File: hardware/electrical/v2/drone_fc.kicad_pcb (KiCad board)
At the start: 0 parts

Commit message: schematic: add MCU decoupling, IMU CS pull-up and INT2 pin
Drops the analog CURRENT_SENSE net: the ESC reports pack current over its serial telemetry, so a second path to the same shunt earned nothing and cost an ADC pin. J1 pin 6 and the MCU ADC pin are marked no-connect. Adds decoupling the module supply was missing entirely (4.7 uF bulk plus 100 nF per rail), a 1 uF local input cap at the LDO, and a 10k pull-up on IMU_CS so the IMU does not see spurious SPI while the MCU is in reset. Adds the missing INT2 pin 14 to the ICM-42688-P symbol, which is a 14-pad part, and marks it no-connect. ERC is clean: 0 errors, remaining warnings are library sync only. PCB layout is still work in progress and has known DRC violations.
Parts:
- added C1: 100nF_BOOT, Capacitor_SMD:C_0402_1005Metric, F.Cu at (63.0, 104.9)
- added C10: 1uF, Capacitor_SMD:C_0603_1608Metric, F.Cu at (56.1, 110.4)
- added C2: 10uF_50V, Capacitor_SMD:C_0805_2012Metric, F.Cu at (71.8, 104.6)
- added C3: 22uF_10V, Capacitor_SMD:C_0805_2012Metric, F.Cu at (71.8, 107.6)
- added C5: 100nF, Capacitor_SMD:C_0402_1005Metric, F.Cu at (63.0, 106.9)
- added C6: 10nF, Capacitor_SMD:C_0402_1005Metric, F.Cu at (63.0, 108.8)
- added D1: Green_Status, LED_SMD:LED_0402_1005Metric, F.Cu at (59.8, 110.1)
- added D2: Blue_Radio, LED_SMD:LED_0402_1005Metric, F.Cu at (59.8, 112.1)
- added J1: ESC_4IN1_JST_SH, drone_fc_v2_footprints:JST_SH_SM08B-SRSS-TB_1x08-1MP_P1.00mm_Horizontal, F.Cu at (115.0, 89.0)
- added J3: Cortex_SWD_10P, Connector_PinHeader_1.27mm:PinHeader_2x05_P1.27mm_Vertical_SMD, F.Cu at (86.0, 86.8)
- added L1: 15uH, Inductor_SMD:L_0805_2012Metric, F.Cu at (51.8, 110.5)
- added R10: 10k, Resistor_SMD:R_0402_1005Metric, F.Cu at (63.0, 98.9)
- added R11: 88.7K, Resistor_SMD:R_0402_1005Metric, F.Cu at (63.0, 100.9)
- added R12: 22.1K, Resistor_SMD:R_0402_1005Metric, F.Cu at (63.0, 102.9)
- added R3: 1k_1%, Resistor_SMD:R_0402_1005Metric, F.Cu at (63.0, 89.0)
- added R4: 1k_1%, Resistor_SMD:R_0402_1005Metric, F.Cu at (63.0, 91.0)
- added R7: 10k, Resistor_SMD:R_0402_1005Metric, F.Cu at (63.0, 93.0)
- added R8: 10k, Resistor_SMD:R_0402_1005Metric, F.Cu at (63.0, 95.0)
- added R9: 10k, Resistor_SMD:R_0402_1005Metric, F.Cu at (63.0, 97.0)
- added TVS1: SMAJ24A, Diode_SMD:D_SMA, F.Cu at (53.6, 106.8)
- added U1: MDBT53-P1M, drone_fc_v2_footprints:MDBT53-P1M, F.Cu at (100.0, 90.5)
- added U2: ICM-42688-P, drone_fc_v2_footprints:LGA-14_2.5x3.0mm_P0.5mm_ICM42688P, F.Cu at (72.0, 111.6)
- added U3: LMR50410_Buck, Package_TO_SOT_SMD:SOT-23-6, F.Cu at (67.0, 105.5)
- added U4: TLV75533PDBVR, Package_TO_SOT_SMD:SOT-23-5, F.Cu at (67.0, 110.1)
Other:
- board outline added: 38 x 38 mm
- copper layers 0 -> 4
- board text added: "ANTENNA ZONE - NO COPPER"

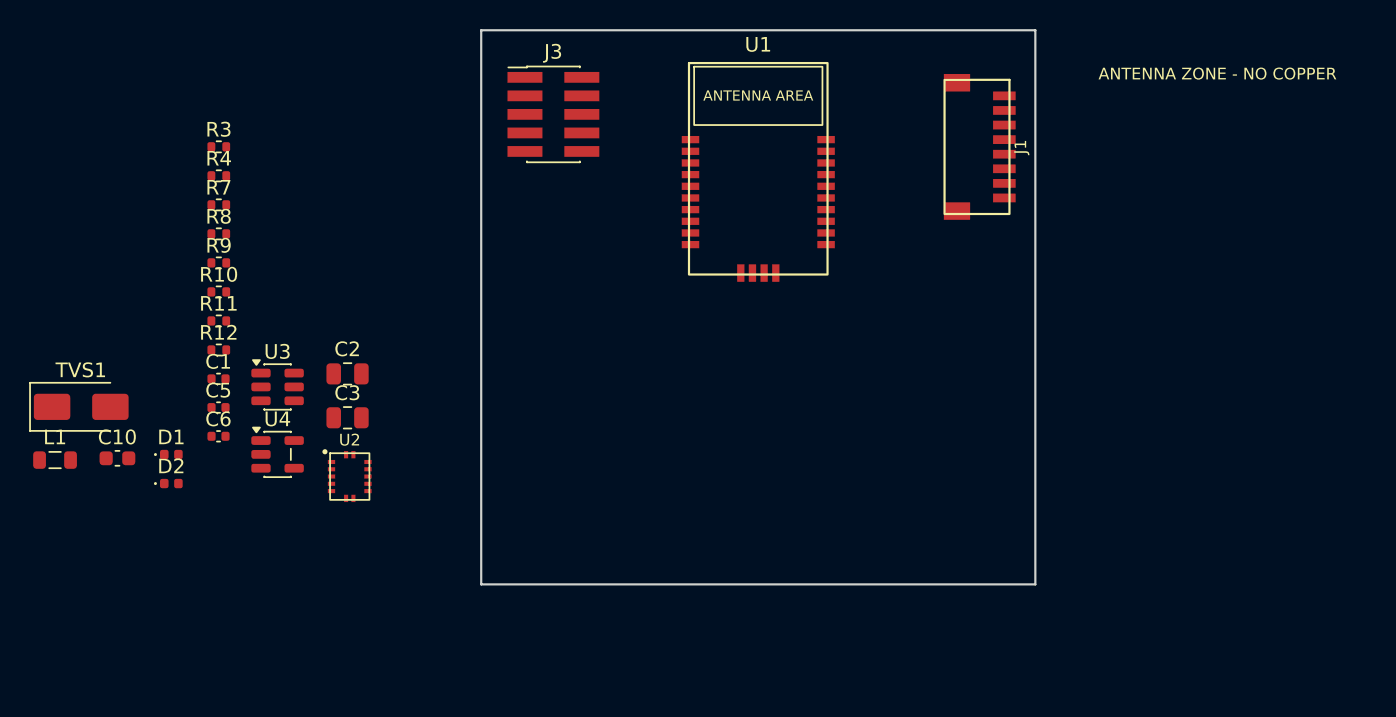
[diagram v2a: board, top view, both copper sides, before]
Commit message: layout: establish stack-compatible FC placement
Define the 20 mm ESC mounting pattern and board outline, place the flight-controller components around the stack, and preserve the MDBT53 antenna keepout at the board edge. Add labelled GND, VBAT, +4V, and +3V3 schematic test points with matching board pads. Repair the MDBT53 courtyard and route the first buck switch-node and +4V segments.\n\nERC is clean. PCB DRC has no electrical or mechanical errors; remaining findings are silkscreen-only while routing is in progress.
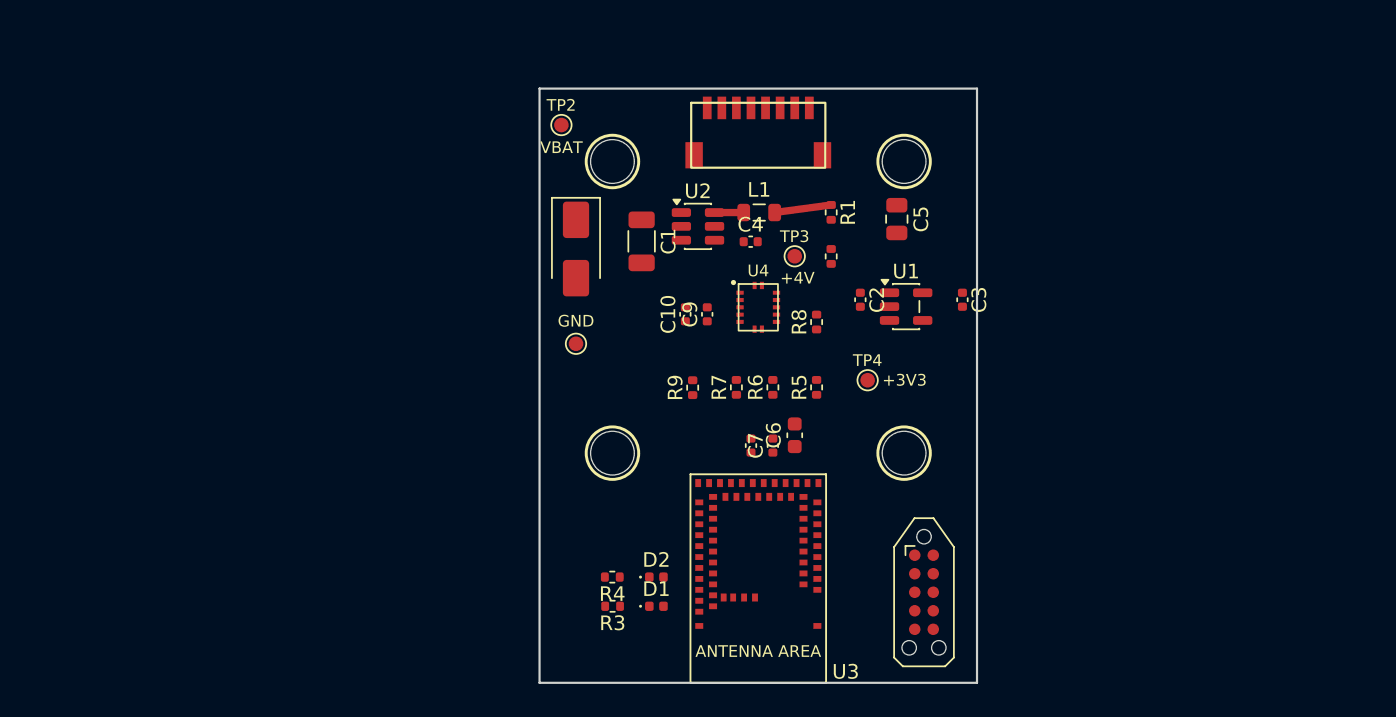
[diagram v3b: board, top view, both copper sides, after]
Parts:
- removed J3: Cortex_SWD_10P, Connector_PinHeader_1.27mm:PinHeader_2x05_P1.27mm_Vertical_SMD
- removed R10: 10k, Resistor_SMD:R_0402_1005Metric
- removed R11: 88.7K, Resistor_SMD:R_0402_1005Metric
- removed R12: 22.1K, Resistor_SMD:R_0402_1005Metric
- added C4: 100nF, Capacitor_SMD:C_0402_1005Metric, F.Cu at (99.5, 95.5)
- added C7: 100nF, Capacitor_SMD:C_0402_1005Metric, F.Cu at (101.0, 109.5)
- added C8: 100nF, Capacitor_SMD:C_0402_1005Metric, F.Cu at (99.5, 109.5)
- added C9: 100nF, Capacitor_SMD:C_0402_1005Metric, F.Cu at (96.5, 100.5)
- added H1: M2 soft mount, MountingHole_3.0mm, F.Cu at (90.0, 90.0)
- added H2: M2 soft mount, MountingHole_3.0mm, F.Cu at (110.0, 90.0)
- added H3: M2 soft mount, MountingHole_3.0mm, F.Cu at (90.0, 110.0)
- added H4: M2 soft mount, MountingHole_3.0mm, F.Cu at (110.0, 110.0)
- added J2: ESC_4IN1_JST_SH, drone_fc_v2_footprints:JST_SH_SM08B-SRSS-TB_1x08-1MP_P1.00mm_Horizontal, F.Cu at (100.0, 88.2)
- added R1: 66.5K, Resistor_SMD:R_0402_1005Metric, F.Cu at (105.0, 93.5)
- added R2: 22.1K, Resistor_SMD:R_0402_1005Metric, F.Cu at (105.0, 96.5)
- added R5: 10k, Resistor_SMD:R_0402_1005Metric, F.Cu at (104.0, 105.5)
- added R6: 10k, Resistor_SMD:R_0402_1005Metric, F.Cu at (101.0, 105.5)
- added TP1: GND, TestPoint:TestPoint_Pad_D1.0mm, F.Cu at (87.5, 102.5)
- added TP2: VBAT, TestPoint:TestPoint_Pad_D1.0mm, F.Cu at (86.5, 87.5)
- added TP3: +4V, TestPoint:TestPoint_Pad_D1.0mm, F.Cu at (102.5, 96.5)
- added TP4: +3V3, TestPoint:TestPoint_Pad_D1.0mm, F.Cu at (107.5, 105.0)
- C1: value 100nF_BOOT -> 10uF; footprint Capacitor_SMD:C_0402_1005Metric -> Capacitor_SMD:C_1206_3216Metric
- C10: value 1uF -> 10nF; footprint Capacitor_SMD:C_0603_1608Metric -> Capacitor_SMD:C_0402_1005Metric
- C2: value 10uF_50V -> 1uF; footprint Capacitor_SMD:C_0805_2012Metric -> Capacitor_SMD:C_0402_1005Metric
- C3: value 22uF_10V -> 1uF; footprint Capacitor_SMD:C_0805_2012Metric -> Capacitor_SMD:C_0402_1005Metric
- C5: value 100nF -> 22uF; footprint Capacitor_SMD:C_0402_1005Metric -> Capacitor_SMD:C_0805_2012Metric
- C6: value 10nF -> 4.7uF; footprint Capacitor_SMD:C_0402_1005Metric -> Capacitor_SMD:C_0603_1608Metric
- J1: value ESC_4IN1_JST_SH -> Cortex_SWD_10P; footprint drone_fc_v2_footprints:JST_SH_SM08B-SRSS-TB_1x08-1MP_P1.00mm_Horizontal -> Connector:Tag-Connect_TC2050-IDC-NL_2x05_P1.27mm_Vertical
- R3, R4: value 1k_1% -> 1k
- U1: value MDBT53-P1M -> TLV75533PDBVR; footprint drone_fc_v2_footprints:MDBT53-P1M -> Package_TO_SOT_SMD:SOT-23-5
- U2: value ICM-42688-P -> LMR50410_Buck; footprint drone_fc_v2_footprints:LGA-14_2.5x3.0mm_P0.5mm_ICM42688P -> Package_TO_SOT_SMD:SOT-23-6
- U3: value LMR50410_Buck -> MDBT53-P1M; footprint Package_TO_SOT_SMD:SOT-23-6 -> drone_fc_v2_footprints:MDBT53-P1M
- U4: value TLV75533PDBVR -> ICM-42688-P; footprint Package_TO_SOT_SMD:SOT-23-5 -> drone_fc_v2_footprints:LGA-14_2.5x3.0mm_P0.5mm_ICM42688P
- moved L1 51.2 mm to (100.1, 93.5)
- moved C5 48.3 mm to (109.5, 94.0), turned to -90 degrees
- moved C3 42.9 mm to (114.0, 99.5), turned to -90 degrees
- moved R3 41.5 mm to (90.0, 120.5), turned to 180 degrees
- moved R8 41.4 mm to (104.0, 101.0), turned to 90 degrees
- moved C10 40.2 mm to (95.0, 100.5), turned to 90 degrees
- moved C6 39.5 mm to (102.5, 108.8), turned to 90 degrees
- moved R4 38.5 mm to (90.0, 118.5), turned to 180 degrees
- moved R7 37.6 mm to (98.5, 105.5), turned to 90 degrees
- moved TVS1 35.6 mm to (87.5, 96.0), turned to -90 degrees
- moved C2 35.5 mm to (107.0, 99.5), turned to -90 degrees
- moved U3 35.5 mm to (100.0, 118.6)
- moved D1 34.9 mm to (93.0, 120.5)
- moved U4 34.5 mm to (100.0, 100.0)
- moved D2 33.9 mm to (93.0, 118.5)
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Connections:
- C1 pad 1: Net-(U3-SW) -> /VBAT
- C1 pad 2: Net-(U3-BOOT) -> GND
- C2 pad 1: /VBAT -> /+4V
- C3 pad 1: /+5V -> /+3V3
- C5 pad 1: /+3V3 -> /+4V
- J1 pad 1: /ESC_M4 -> /+3V3
- J1 pad 2: /ESC_M3 -> /SWDIO
- J1 pad 3: /ESC_M2 -> GND
- J1 pad 4: /ESC_M1 -> /SWDCLK
- J1 pad 5: /ESC_TLM -> GND
- J1 pad 6: /CURRENT_SENSE -> /SWO
- J1 pad 7: GND -> (no net)
- J1 pad 8: /VBAT -> (no net)
- L1 pad 1: Net-(U3-SW) -> Net-(U2-SW)
- L1 pad 2: /+5V -> /+4V
- R7 pad 1: /ESC_M4 -> /ESC_M2
- R8 pad 1: /ESC_M3 -> /+3V3
- R8 pad 2: GND -> /IMU_CS
- R9 pad 1: /ESC_M2 -> /ESC_M1
- U1 pad 1: GND -> /+4V
- U1 pad 2: /+3V3 -> GND
- U1 pad 3: /+3V3 -> /+4V
- U1 pad 5: /nRESET -> /+3V3
- U2 pad 1: /SPI_MISO -> Net-(U2-BOOT)
- U2 pad 2: /IMU_INT1 -> GND
- U2 pad 3: /+3V3 -> Net-(U2-FB)
- U2 pad 4: GND -> /VBAT
- U2 pad 5: GND -> /VBAT
- U2 pad 6: GND -> Net-(U2-SW)
- U3 pad 1: Net-(U3-BOOT) -> GND
- U3 pad 2: GND -> /SWDCLK
- U3 pad 3: Net-(U3-FB) -> /SWO
- U3 pad 4: /VBAT -> /SWDIO
- U3 pad 5: /VBAT -> unconnected-(U3-P0.27_AIN6_VBAT-Pad5)
- U3 pad 6: Net-(U3-SW) -> /nRESET
- U4 pad 1: /+5V -> /SPI_MISO
- U4 pad 3: (no net) -> GND
- U4 pad 4: (no net) -> /IMU_INT1
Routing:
- net /+4V: track 0.00 -> 3.91 mm
- net Net-(U2-SW): track 0.00 -> 2.00 mm
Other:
- board size 38 x 38 mm -> 30 x 40.8 mm
- board text removed: "ANTENNA ZONE - NO COPPER"

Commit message: layout: route ground plane and document progress
Connect the ground plane through local vias and reduce the unrouted-net count to 30. Record the Phase 4 PCB layout milestone in the project status and progress history. Remaining DRC work is limited to silkscreen cleanup and two dangling tracks.
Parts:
- moved TP4 4.47 mm to (105.5, 109.0)
- moved D1 2.25 mm to (92.0, 122.5)
- moved D2 2.25 mm to (92.0, 120.5)
- moved R3 2.25 mm to (89.0, 122.5)
- moved R4 2.25 mm to (89.0, 120.5)
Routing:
- net GND: track 0.00 -> 60.1 mm, vias 0 -> 12
- net /+3V3: track 0.00 -> 30.8 mm, vias 0 -> 3
- net /VBAT: track 0.00 -> 28.0 mm
- net /+4V: track 3.91 -> 20.7 mm
- net Net-(U2-BOOT): track 0.00 -> 7.89 mm
- net /ESC_M2: track 0.00 -> 6.52 mm
- net /ESC_M1: track 0.00 -> 6.50 mm
- added copper zone on In2.Cu, net /+3V3
- added copper zone on In1.Cu, net GND

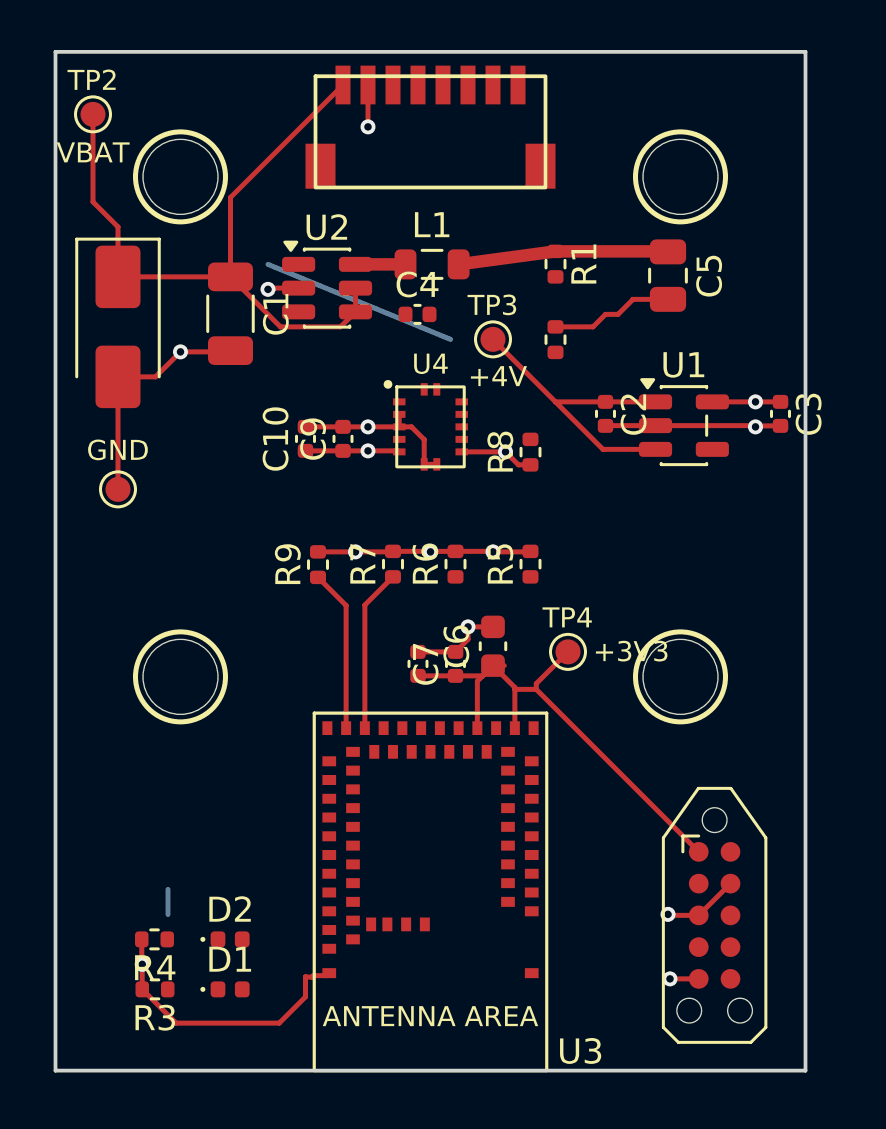
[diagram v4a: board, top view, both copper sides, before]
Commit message: layout: complete routing of the flight controller PCB
Every net on the nRF5340 carrier is now routed: 0 unconnected items, down
from 30 at the end of the previous session. No copper, clearance, short,
drill or dangling-item violations remain. The 23 outstanding DRC findings
are all silkscreen warnings - reference text over pads, label collisions
and text clipped by the board edge - which have no electrical or assembly
consequence on a 30 mm board populated with 0402s.

Also removes an accidental mirror on U2 that a crash-recovery autosave had
introduced. Mirroring a symbol relocates its pin endpoints while the wires
stay put, so every pin had swapped with its opposite across the centreline
(VIN with SW, GND with FB, BOOT with EN) - a real netlist fault rather than
a cosmetic flip. Adds the LMR50410 datasheet alongside the existing TLV755P.
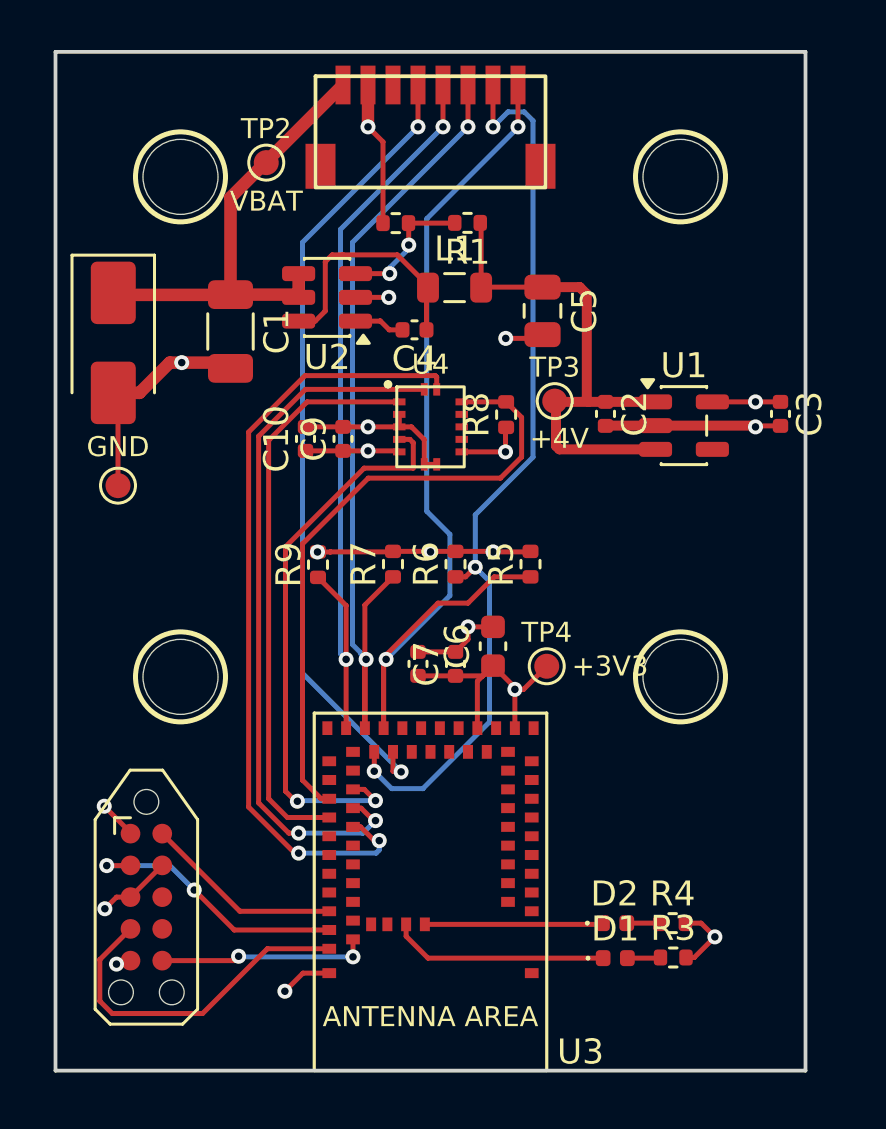
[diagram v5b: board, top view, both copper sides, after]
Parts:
- moved J1 22.7 mm to (88.6, 118.8)
- moved R3 20.8 mm to (109.7, 121.2), turned to 0 degrees
- moved R4 20.7 mm to (109.7, 119.8), turned to 0 degrees
- moved D1 15.5 mm to (107.4, 121.2)
- moved D2 15.4 mm to (107.4, 119.8)
- moved R2 7.91 mm to (98.6, 91.8), turned to 180 degrees
- moved TP2 7.19 mm to (93.4, 89.4)
- moved C5 5.21 mm to (104.5, 95.4)
- moved R1 3.89 mm to (101.5, 91.8), turned to 180 degrees
- moved TP3 3.49 mm to (105.0, 99.0)
- moved R8 1.79 mm to (103.0, 99.5)
- moved L1 1.29 mm to (101.0, 94.4)
- moved TP4 1.03 mm to (104.7, 109.6)
- moved C1 0.71 mm to (92.0, 96.2)
- moved TVS1 0.67 mm to (87.3, 96.6)
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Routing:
- net /ESC_M4: track 0.00 -> 38.6 mm, vias 0 -> 2
- net /ESC_M3: track 0.00 -> 36.5 mm, vias 0 -> 3
- net /ESC_TLM: track 0.00 -> 32.0 mm, vias 0 -> 2
- net /SPI_SCK: track 0.00 -> 31.7 mm, vias 0 -> 2
- net /SPI_MOSI: track 0.00 -> 28.6 mm, vias 0 -> 2
- net /ESC_M2: track 6.52 -> 34.3 mm, vias 0 -> 2
- net /IMU_CS: track 0.00 -> 25.3 mm
- net /ESC_M1: track 6.50 -> 31.2 mm, vias 0 -> 2
- net /SPI_MISO: track 0.00 -> 22.9 mm
- net /IMU_INT1: track 0.00 -> 22.7 mm, vias 0 -> 2
- net /SWDCLK: track 0.00 -> 13.9 mm
- net /VBAT: track 28.0 -> 16.5 mm
- net /SWDIO: track 0.00 -> 10.9 mm, vias 0 -> 2
- net /+3V3: track 30.8 -> 21.1 mm, vias 3 -> 5
- net Net-(D1-A): track 0.00 -> 8.72 mm
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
